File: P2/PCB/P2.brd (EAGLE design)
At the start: 98.7 x 30.5 mm, 33 parts, among them CON1 Volume, CON2 Autosense, CON3 Noritake, IC1 ATMEGA48/88/168-AU, IC2 TPIC6B595DW, IC3 TPIC6B595DW, K1 G6H2-100, Q1 16MHz

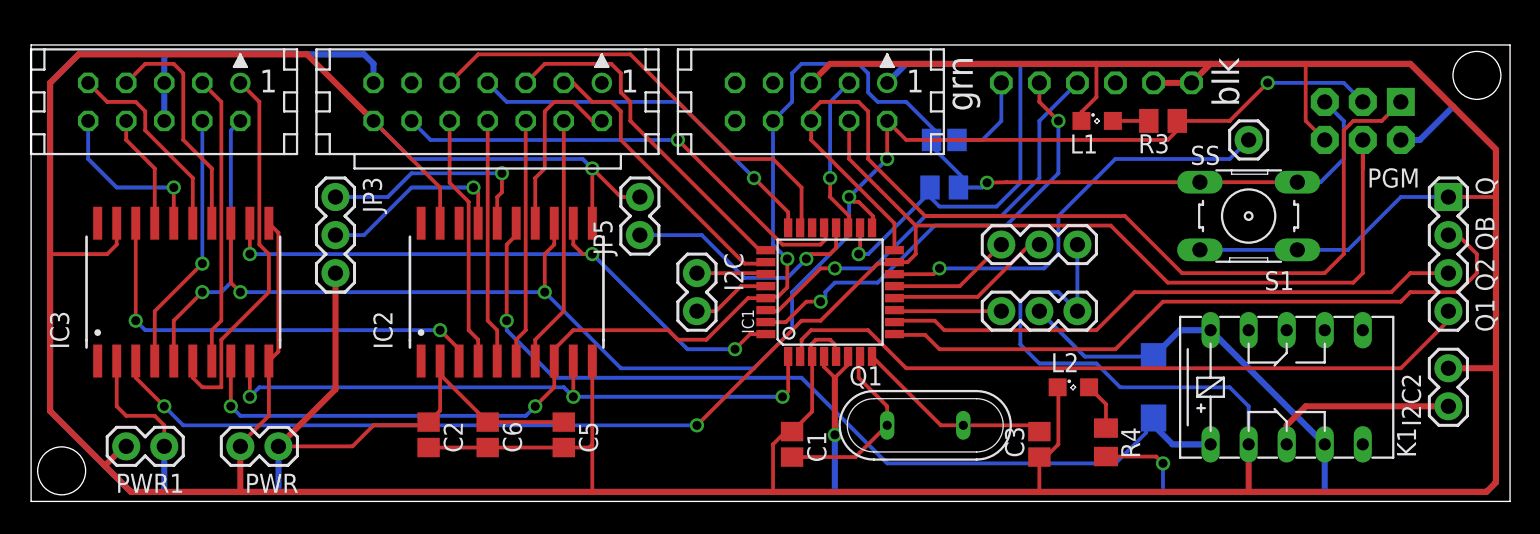
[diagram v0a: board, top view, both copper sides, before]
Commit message: P2 PCB update for peakdetect.
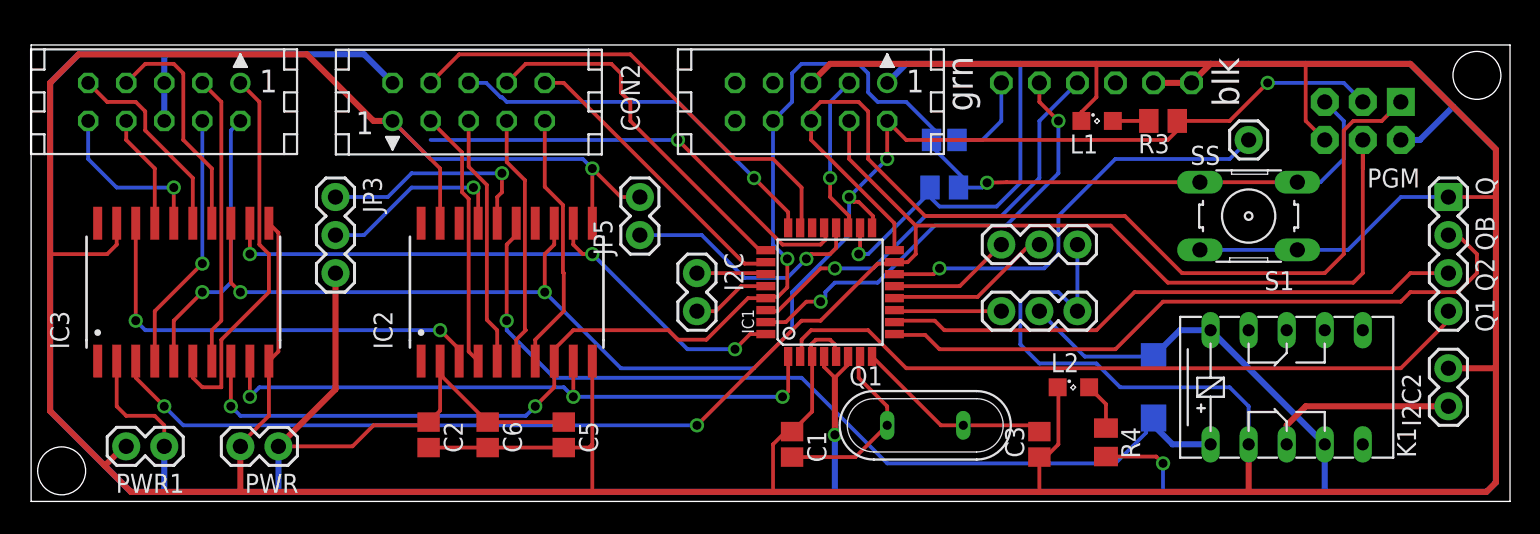
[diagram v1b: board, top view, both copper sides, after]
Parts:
- CON2: value Autosense -> Channels; device con-harting-lars:CON14L -> con-harting-lars:CON10L
- moved CON2 1.27 mm to (29.2, 26.7), turned to 180 degrees
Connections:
- removed net OUT12: CON2.2, IC2.14
- net +5V: now also CON2.2; no longer CON2.13
- net ADC0: now also CON2.4; no longer CON2.9
- net ADC1: now also CON2.6; no longer CON2.7
- net ADC2: now also CON2.8; no longer CON2.5
- net ADC3: now also CON2.10; no longer CON2.3
- net AGND: no longer CON2.12
- net GND: now also CON2.1; no longer CON2.14
- net OUT10: now also CON2.7; no longer CON2.6
- net OUT11: now also CON2.9; no longer CON2.4
- net OUT8: now also CON2.3; no longer CON2.10
- net OUT9: now also CON2.5; no longer CON2.8
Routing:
- net OUT12: track 12.3 -> 0.00 mm
- net AGND: track 32.0 -> 30.2 mm
- net ADC2: track 23.2 -> 24.5 mm
- net ADC1: track 24.7 -> 26.0 mm
- net ADC0: track 30.7 -> 32.0 mm
- net OUT9: track 16.3 -> 16.8 mm
- net OUT8: track 16.8 -> 17.3 mm
- net OUT10: track 16.3 -> 16.8 mm
- net OUT11: track 16.8 -> 17.3 mm
- net GND: track 390.8 -> 390.2 mm
- net +5V: track 340.2 -> 340.7 mm

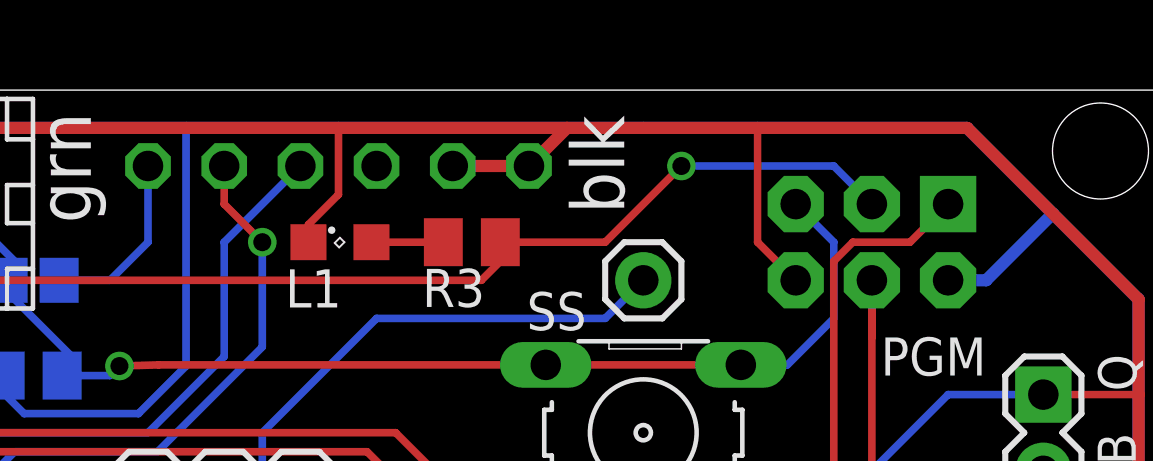
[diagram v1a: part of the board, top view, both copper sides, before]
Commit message: Connect pin 3 of the serial connector to power. Doh.
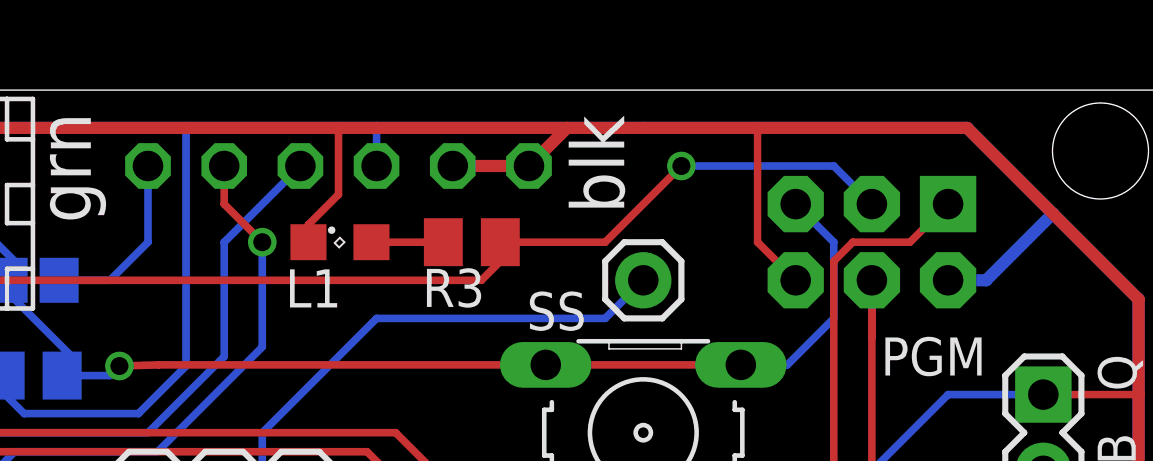
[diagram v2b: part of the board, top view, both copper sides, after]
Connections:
- net +5V: now also JP1.3
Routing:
- net +5V: track 340.7 -> 342.0 mm
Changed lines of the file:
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@@
 <?xml version="1.0" encoding="utf-8"?>
 <!DOCTYPE eagle SYSTEM "eagle.dtd">
-<eagle version="8.6.1">
+<eagle version="8.7.1">
 <drawing>
 <settings>
@@
 <wire x1="1.27" y1="6.0325" x2="6.6675" y2="0.635" width="0.4064" layer="16"/>
 <wire x1="8.89" y1="0.635" x2="6.6675" y2="0.635" width="0.4064" layer="16"/>
-<wire x1="66.04" y1="29.21" x2="92.075" y2="29.21" width="0.4064" layer="16"/>
+<wire x1="66.04" y1="29.21" x2="72.39" y2="29.21" width="0.4064" layer="16"/>
+<wire x1="72.39" y1="29.21" x2="92.075" y2="29.21" width="0.4064" layer="16"/>
 <wire x1="92.075" y1="29.21" x2="94.9325" y2="26.3525" width="0.4064" layer="16"/>
 <wire x1="94.9325" y1="26.3525" x2="97.79" y2="23.495" width="0.4064" layer="16"/>
@@
 <contactref element="CON2" pad="2"/>
 <wire x1="22.225" y1="29.845" x2="24.13" y2="27.94" width="0.4064" layer="16"/>
+<contactref element="JP1" pad="3"/>
+<wire x1="72.39" y1="27.94" x2="72.39" y2="29.21" width="0.254" layer="16"/>
 </signal>
 <signal name="MOSI">

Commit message: Flip channel connector
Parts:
- moved CON2 1.90 mm to (31.1, 26.7), turned to 0 degrees
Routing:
- net AGND: track 30.2 -> 0.00 mm, vias 1 -> 0
- net +5V: track 342.0 -> 360.7 mm
- net GND: track 390.2 -> 406.0 mm
- net OUT11: track 17.3 -> 28.5 mm
- net ADC0: track 32.0 -> 20.9 mm
- net ADC3: track 19.8 -> 28.6 mm, vias 0 -> 1
- net OUT9: track 16.8 -> 24.9 mm
- net OUT8: track 17.3 -> 21.1 mm, vias 0 -> 1
- net ADC1: track 26.0 -> 22.4 mm, vias 1 -> 0
- net OUT10: track 16.8 -> 20.1 mm
- net RCK: track 42.5 -> 43.7 mm
- net OUT13: track 60.9 -> 60.2 mm
- net ADC2: track 24.5 -> 24.4 mm, vias 0 -> 1

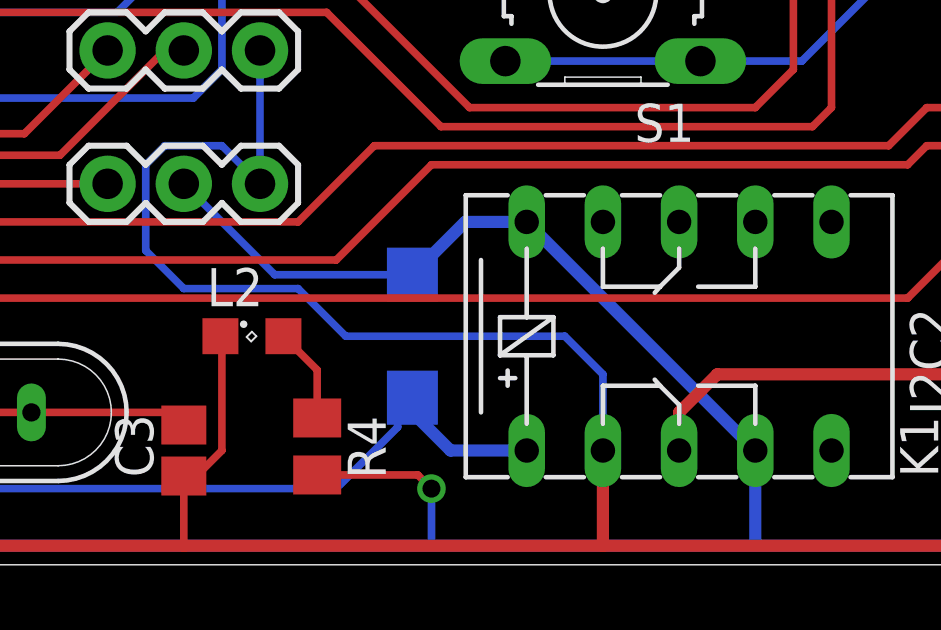
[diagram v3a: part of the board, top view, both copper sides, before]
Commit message: Working version with heavily patched PCB
- ADC6 does not work as /SS for Noritake, use B0.
- Relay connected wrong (internal diode!)
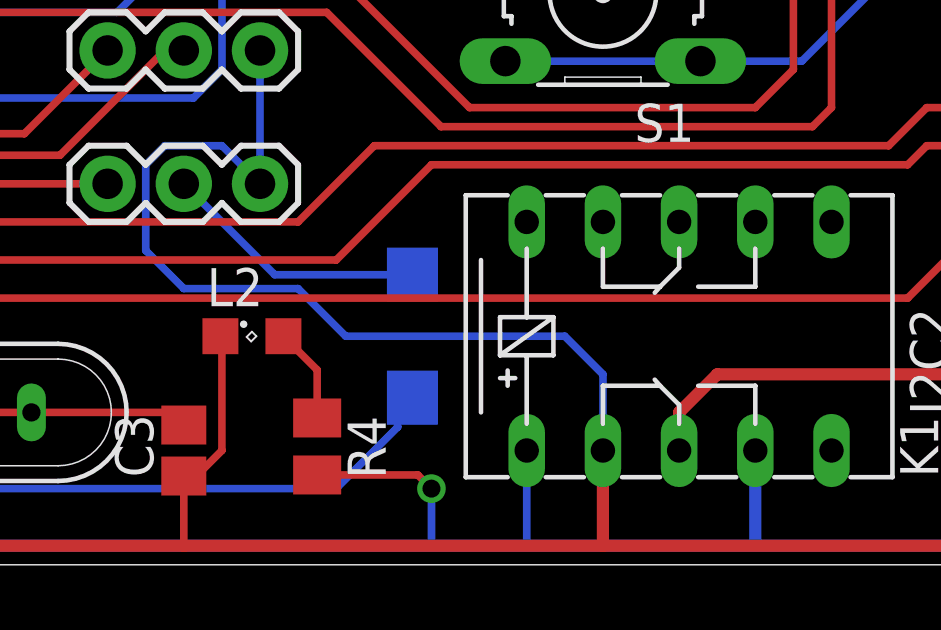
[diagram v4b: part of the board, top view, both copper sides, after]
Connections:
- removed net N$11: IC2.16, JP3.1
- new net OUT14: D1.A, IC2.16, JP3.1, K1.10
- net +5V: now also K1.1; no longer K1.10
- net OUT13: no longer D1.A, K1.1
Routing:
- net OUT14: track 0.00 -> 15.2 mm, vias 0 -> 1
- net N$11: track 15.2 -> 0.00 mm, vias 1 -> 0
- net +5V: track 360.7 -> 348.6 mm
- net OUT13: track 60.2 -> 54.9 mm
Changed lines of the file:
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@@
 <wire x1="16.51" y1="0.635" x2="53.6575" y2="0.635" width="0.4064" layer="16"/>
 <wire x1="53.6575" y1="0.635" x2="75.565" y2="0.635" width="0.4064" layer="16"/>
-<wire x1="75.565" y1="0.635" x2="86.36" y2="0.635" width="0.4064" layer="16"/>
+<wire x1="75.565" y1="0.635" x2="78.74" y2="0.635" width="0.4064" layer="16"/>
+<wire x1="78.74" y1="0.635" x2="86.36" y2="0.635" width="0.4064" layer="16"/>
 <wire x1="8.89" y1="3.675" x2="8.89" y2="0.635" width="0.4064" layer="16"/>
 <wire x1="1.27" y1="27.94" x2="3.175" y2="29.845" width="0.4064" layer="16"/>
@@
 <wire x1="27.305" y1="9.37" x2="27.305" y2="8.47" width="0.254" layer="1"/>
 <wire x1="27.305" y1="8.47" x2="30.48" y2="5.295" width="0.254" layer="1"/>
-<contactref element="K1" pad="10"/>
-<contactref element="D1" pad="K"/>
 <contactref element="K1" pad="S1"/>
 <wire x1="5.715" y1="9.37" x2="5.715" y2="6.35" width="0.254" layer="1"/>
@@
 <wire x1="97.155" y1="0.635" x2="86.36" y2="0.635" width="0.4064" layer="16"/>
 <wire x1="86.36" y1="3.81" x2="86.36" y2="0.635" width="0.4064" layer="16"/>
-<wire x1="78.74" y1="11.43" x2="86.36" y2="3.81" width="0.4064" layer="16"/>
-<wire x1="78.74" y1="11.43" x2="76.69" y2="11.43" width="0.4064" layer="16"/>
-<wire x1="76.69" y1="11.43" x2="74.93" y2="9.67" width="0.4064" layer="16"/>
 <wire x1="66.04" y1="29.21" x2="58.42" y2="29.21" width="0.4064" layer="16"/>
 <wire x1="58.42" y1="29.21" x2="57.15" y2="27.94" width="0.4064" layer="16"/>
@@
 <wire x1="20.32" y1="7.485" x2="16.51" y2="3.675" width="0.4064" layer="1"/>
 <contactref element="JP4" pad="2"/>
-<wire x1="74.93" y1="9.67" x2="70.34" y2="9.67" width="0.254" layer="16"/>
-<wire x1="70.34" y1="9.67" x2="67.31" y2="12.7" width="0.254" layer="16"/>
+<wire x1="67.31" y1="12.7" x2="70.34" y2="9.67" width="0.254" layer="16"/>
 <contactref element="IC1" pad="18"/>
 <wire x1="66.04" y1="29.21" x2="66.04" y2="21.2725" width="0.254" layer="16"/>
@@
 <wire x1="37.465" y1="25.4" x2="36.195" y2="25.4" width="0.4064" layer="16"/>
 <wire x1="38.1" y1="29.21" x2="38.1" y2="26.035" width="0.4064" layer="16"/>
+<contactref element="K1" pad="1"/>
+<contactref element="D1" pad="K"/>
+<wire x1="70.34" y1="9.67" x2="74.93" y2="9.67" width="0.254" layer="16"/>
+<wire x1="78.74" y1="3.81" x2="78.74" y2="0.635" width="0.254" layer="16"/>
+<wire x1="75.11" y1="2.995" x2="74.93" y2="9.67" width="0" layer="19" extent="1-16"/>
 </signal>
 <signal name="MOSI">
@@
 <signal name="OUT13">
 <contactref element="IC2" pad="15"/>
-<contactref element="K1" pad="1"/>
-<contactref element="D1" pad="A"/>
-<wire x1="74.93" y1="5.57" x2="74.93" y2="5.08" width="0.4064" layer="16"/>
-<wire x1="74.93" y1="5.08" x2="76.2" y2="3.81" width="0.4064" layer="16"/>
-<wire x1="76.2" y1="3.81" x2="78.74" y2="3.81" width="0.4064" layer="16"/>
-<wire x1="74.93" y1="5.57" x2="74.44" y2="5.57" width="0.254" layer="16"/>
 <via x="32.7025" y="11.43" extent="1-16" drill="0.6"/>
 <wire x1="32.7025" y1="11.43" x2="32.7025" y2="17.4625" width="0.254" layer="1"/>
@@
 <wire x1="47.39" y1="14.37" x2="45.72" y2="12.7" width="0.254" layer="1"/>
 </signal>
-<signal name="N$11">
+<signal name="OUT14">
 <contactref element="IC2" pad="16"/>
 <contactref element="JP3" pad="1"/>
@@
 <wire x1="23.8125" y1="20.32" x2="25.4" y2="21.9075" width="0.254" layer="16"/>
 <wire x1="25.4" y1="21.9075" x2="31.4325" y2="21.9075" width="0.254" layer="16"/>
+<contactref element="D1" pad="A"/>
+<contactref element="K1" pad="10"/>
+<wire x1="74.93" y1="5.57" x2="76.69" y2="5.57" width="0" layer="19" extent="1-16"/>
+<wire x1="76.69" y1="5.57" x2="77.47" y2="6.35" width="0" layer="19" extent="1-16"/>
+<wire x1="77.47" y1="6.35" x2="78.74" y2="11.43" width="0" layer="19" extent="16-16"/>
+<wire x1="31.115" y1="18.57" x2="74.93" y2="5.57" width="0" layer="19" extent="1-16"/>
 </signal>
 <signal name="N$12">
